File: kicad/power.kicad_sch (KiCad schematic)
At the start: 49 parts, among them J4 TYPE-C-31-M-12, Q7 BC847BW,115, U10 MC34063AD, U11 MC34063AD, U12 XC6206P332MR-G, U13 TPS2116DRLR, U9 TPD4S012DRYR

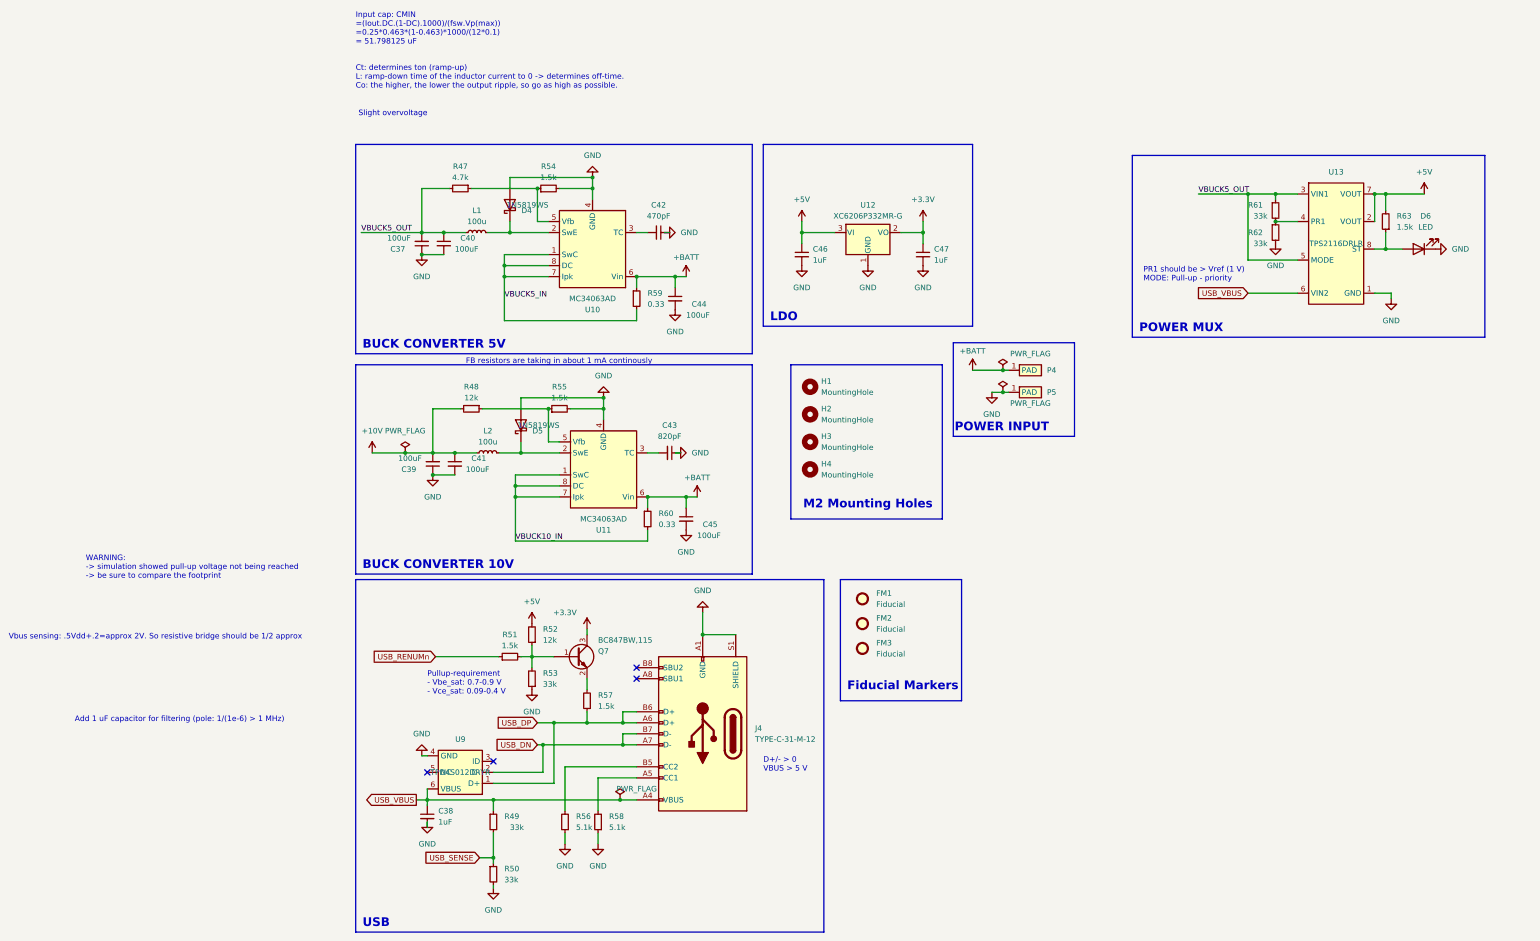
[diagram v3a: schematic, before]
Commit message: [kicad] Added different ESD protection device, silkscreen indication on the back, [review] Added pdf file and images of the front and back as well as 3d images
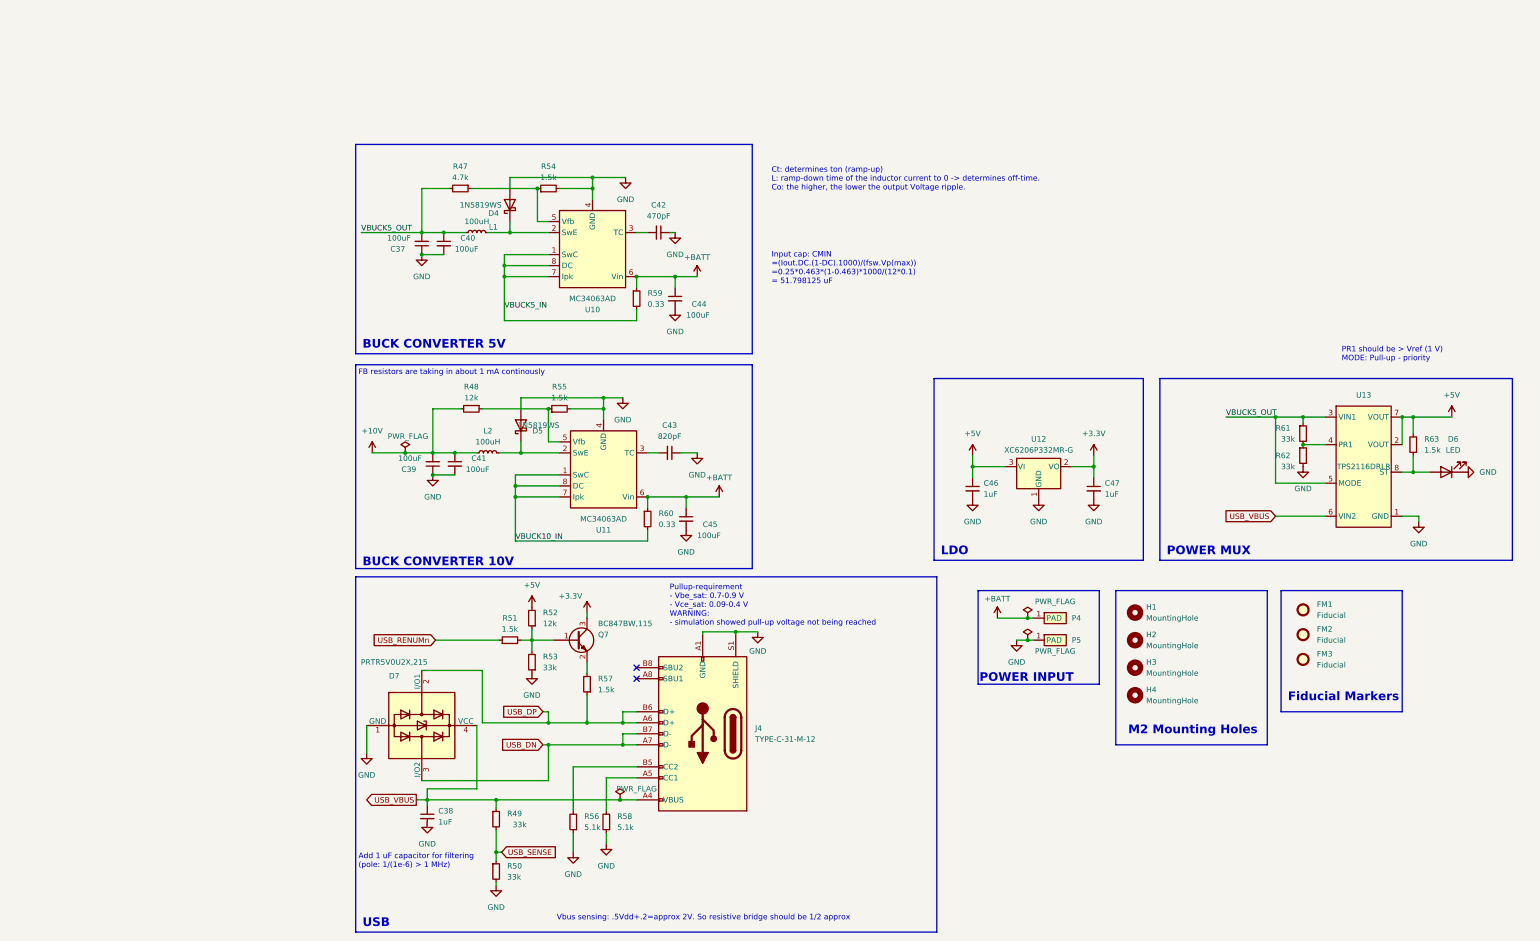
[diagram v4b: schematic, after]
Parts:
- removed U9: TPD4S012DRYR, bldc:TI_R-PUSON-N6, symbol bldc:TPD4S012DRYR
- added D7: PRTR5V0U2X,215, Package_TO_SOT_SMD:SOT-143, symbol Power_Protection:PRTR5V0U2X
- L1, L2: value 100u -> 100uH
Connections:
- net GND: now also D7.1 (GND)
- net USB_DN: now also D7.3 (I/O2)
- net USB_DP: now also D7.2 (I/O1)
- net USB_VBUS: now also D7.4 (VCC)
- no-connect marks 4 -> 2
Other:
- note added: "Ct: determines ton (ramp-up) L: ramp-down time of the inductor current to 0 -> determines off-time. Co: the higher, the lower the output Voltage ripple."
- note added: "Pullup-requirement - Vbe_sat: 0.7-0.9 V - Vce_sat: 0.09-0.4 V WARNING: - simulation showed pull-up voltage not being reached"
- note removed: "Ct: determines ton (ramp-up) L: ramp-down time of the inductor current to 0 -> determines off-time. Co: the higher, the lower the output ripple, so go as high as possible."
- note removed: "D+/- > 0 VBUS > 5 V"
- note removed: "Pullup-requirement - Vbe_sat: 0.7-0.9 V - Vce_sat: 0.09-0.4 V"
- note removed: "Slight overvoltage"
- note removed: "WARNING: -> simulation showed pull-up voltage not being reached -> be sure to compare the footprint"
- company: Igor Wolfs -> IW
- moved on the sheet: C46, C47, D6, FM1, FM2, FM3, H1, H2, H3, H4, P4, P5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

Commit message: [kicad] Added testpoints, added 1 amp fuses at 2 buck converters
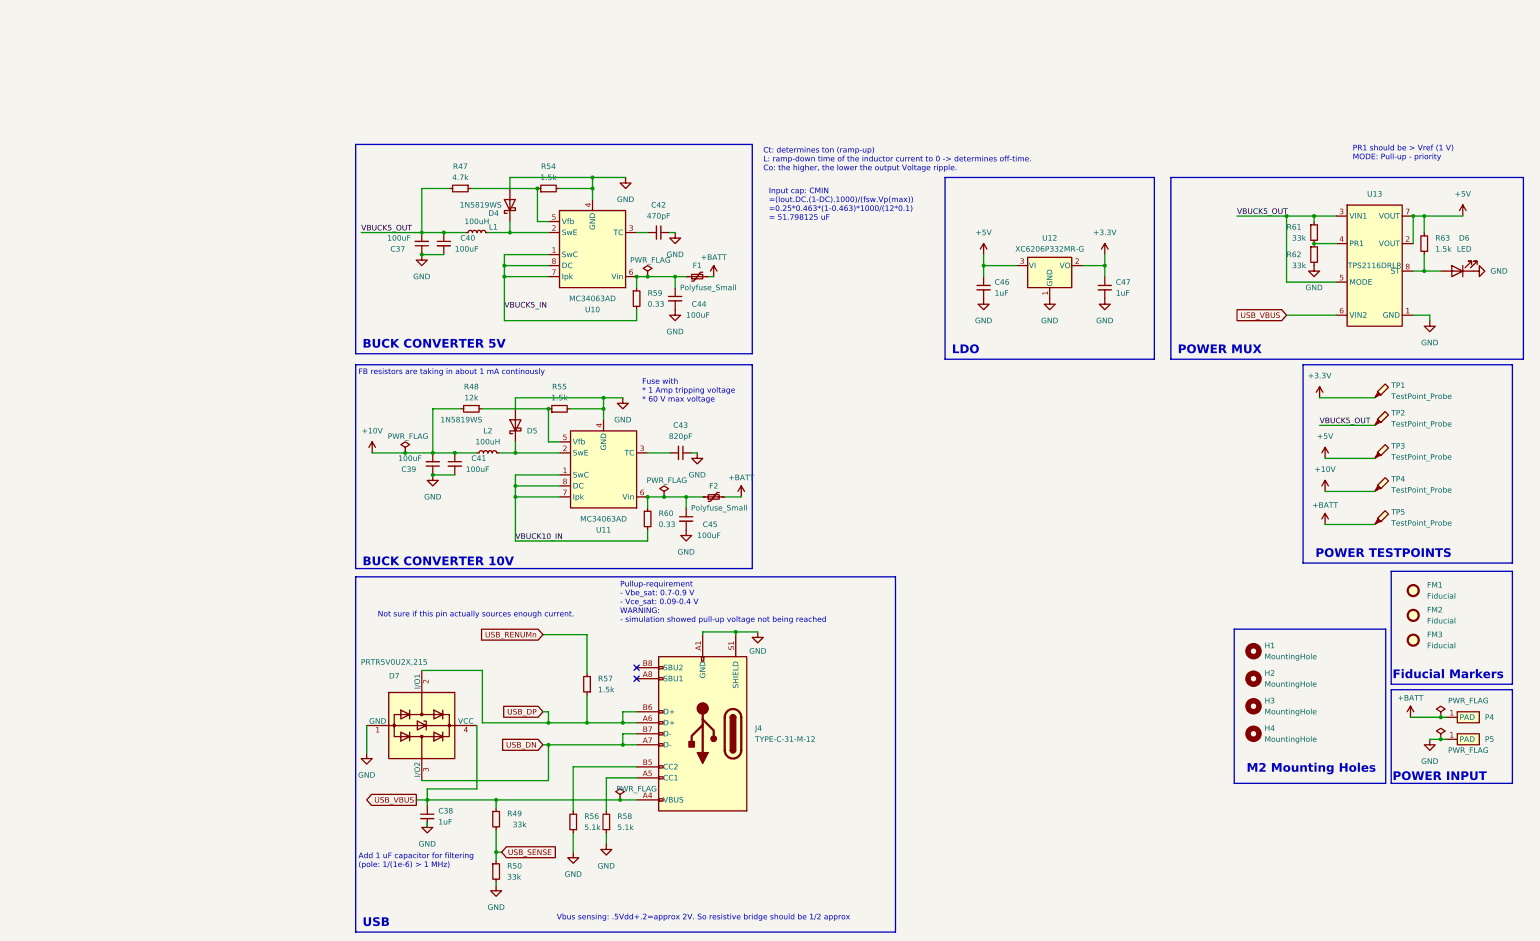
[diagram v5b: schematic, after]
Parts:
- removed Q7: BC847BW,115, Package_TO_SOT_SMD:SOT-323_SC-70, symbol Transistor_BJT:BC847
- removed R51: 1.5k, Resistor_SMD:R_0805_2012Metric, symbol Device:R_Small
- removed R52: 12k, Resistor_SMD:R_0603_1608Metric, symbol Device:R_Small
- removed R53: 33k, Resistor_SMD:R_0603_1608Metric, symbol Device:R_Small
- added F1, F2: Polyfuse_Small, Fuse:Fuse_1812_4532Metric, symbol Device:Polyfuse_Small
- added TP1, TP2, TP3, TP4, TP5: TestPoint_Probe, TestPoint:TestPoint_THTPad_D1.0mm_Drill0.5mm, symbol Connector:TestPoint_Probe
- C42, C43: footprint Capacitor_SMD:C_0805_2012Metric -> Capacitor_SMD:C_0805_2012Metric_Pad1.18x1.45mm_HandSolder
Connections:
- net +10V: now also TP4.1
- net +3.3V: now also TP1.1
- net +5V: now also TP3.1
- net +BATT: now also F1.2, F2.2, TP5.1; no longer C44.1, C45.1, R59.1, R60.1, U10.6 (Vin), U11.6 (Vin)
- net USB_RENUMn: now also R57.2
- net VBUCK5_OUT: now also TP2.1
- new net: C45.1, F2.1, R60.1, U11.6 (Vin)
- new net: C44.1, F1.1, R59.1, U10.6 (Vin)
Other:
- note added: "Fuse with * 1 Amp tripping voltage * 60 V max voltage"
- note added: "Not sure if this pin actually sources enough current."
- moved on the sheet: C43, C46, C47, D5, D6, FM1, FM2, FM3, H1, H2, H3, H4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

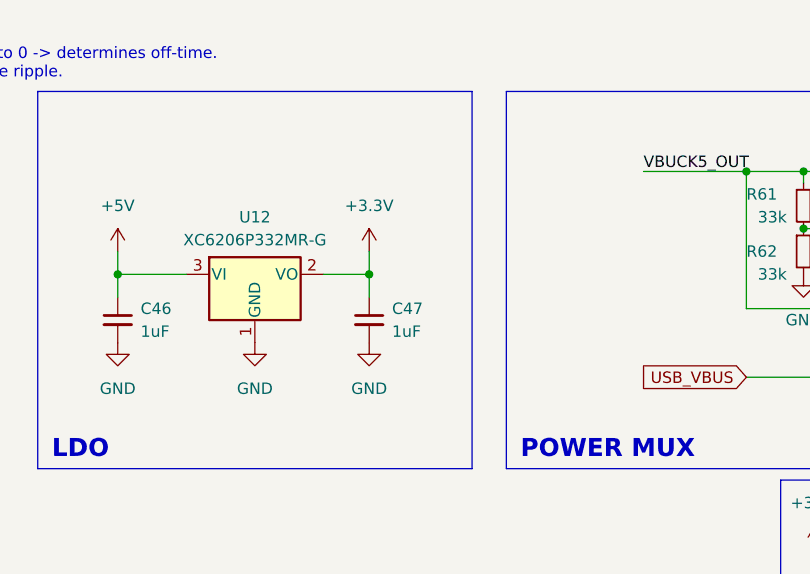
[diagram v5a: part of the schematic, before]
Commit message: [kicad] Added power and keepalive LED | TODO: Add extra mcu output
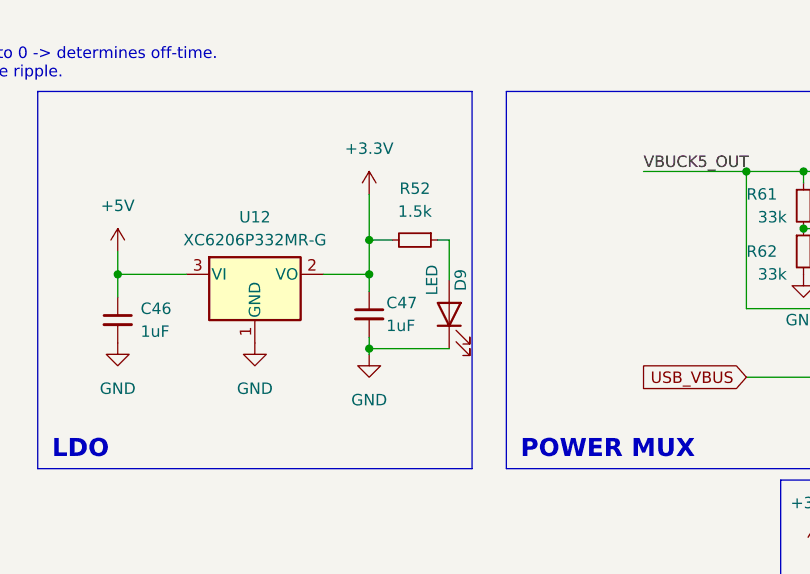
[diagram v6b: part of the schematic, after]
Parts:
- added D9: LED, LED_SMD:LED_0805_2012Metric, symbol Device:LED
- added R52: 1.5k, Resistor_SMD:R_0805_2012Metric, symbol Device:R_Small
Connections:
- net +3.3V: now also R52.2
- net GND: now also D9.1 (K)
- new net: D9.2 (A), R52.1
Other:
- moved on the sheet: C47
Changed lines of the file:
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@@
   (junction (at 50.8 34.29) (diameter 0) (color 0 0 0 0)
   )
+  (junction (at 187.96 38.1) (diameter 0) (color 0 0 0 0)
+  )
   (junction (at 52.07 85.09) (diameter 0) (color 0 0 0 0)
   )
@@
   )
   (junction (at 33.02 85.09) (diameter 0) (color 0 0 0 0)
+  )
+  (junction (at 187.96 50.165) (diameter 0) (color 0 0 0 0)
   )
   (junction (at 91.44 95.25) (diameter 0) (color 0 0 0 0)
@@
     (stroke (width 0) (type default))
   )
+  (wire (pts (xy 187.96 50.8) (xy 187.96 50.165))
+    (stroke (width 0) (type default))
+  )
   (wire (pts (xy 77.47 21.59) (xy 69.85 21.59))
     (stroke (width 0) (type default))
@@
     (stroke (width 0) (type default))
   )
+  (wire (pts (xy 187.96 50.165) (xy 187.96 48.895))
+    (stroke (width 0) (type default))
+  )
   (wire (pts (xy 52.07 105.41) (xy 52.07 95.25))
     (stroke (width 0) (type default))
@@
     (stroke (width 0) (type default))
   )
+  (wire (pts (xy 195.58 38.1) (xy 196.85 38.1))
+    (stroke (width 0) (type default))
+  )
   (wire (pts (xy 266.7 151.13) (xy 265.43 151.13))
     (stroke (width 0) (type default))
@@
     (stroke (width 0) (type default))
   )
+  (wire (pts (xy 187.96 38.1) (xy 187.96 41.91))
+    (stroke (width 0) (type default))
+  )
   (wire (pts (xy 33.02 85.09) (xy 38.1 85.09))
     (stroke (width 0) (type default))
@@
     (stroke (width 0) (type default))
   )
+  (wire (pts (xy 187.96 50.165) (xy 196.85 50.165))
+    (stroke (width 0) (type default))
+  )
   (wire (pts (xy 52.07 105.41) (xy 82.55 105.41))
     (stroke (width 0) (type default))
@@
     (stroke (width 0) (type default))
   )
-  (wire (pts (xy 187.96 41.91) (xy 187.96 44.45))
+  (wire (pts (xy 187.96 41.91) (xy 187.96 43.815))
     (stroke (width 0) (type default))
   )
@@
     (stroke (width 0) (type default))
   )
+  (wire (pts (xy 196.85 38.1) (xy 196.85 42.545))
+    (stroke (width 0) (type default))
+  )
   (wire (pts (xy 82.55 102.87) (xy 82.55 105.41))
     (stroke (width 0) (type default))
@@
     (stroke (width 0) (type default))
   )
-  (wire (pts (xy 187.96 39.37) (xy 187.96 41.91))
+  (wire (pts (xy 187.96 33.02) (xy 187.96 38.1))
+    (stroke (width 0) (type default))
+  )
+  (wire (pts (xy 187.96 38.1) (xy 190.5 38.1))
     (stroke (width 0) (type default))
   )
@@
     )
   )
-  (symbol (lib_id "Device:C_Small") (at 187.96 46.99 0) (unit 1)
-    (in_bom yes) (on_board yes) (dnp no) (fields_autoplaced)
-    (property "Reference" "C47" (at 190.5 45.7263 0)
-      (effects (font (size 1.27 1.27)) (justify left))
-    )
-    (property "Value" "1uF" (at 190.5 48.2663 0)
-      (effects (font (size 1.27 1.27)) (justify left))
-    )
-    (property "Footprint" "Capacitor_SMD:C_1206_3216Metric" (at 187.96 46.99 0)
-      (effects (font (size 1.27 1.27)) hide)
-    )
-    (property "Datasheet" "https://wmsc.lcsc.com/wmsc/upload/file/pdf/v2/lcsc/2304140030_Samsung-Electro-Mechanics-CL31B105KBHNNNE_C1848.pdf" (at 187.96 46.99 0)
-      (effects (font (size 1.27 1.27)) hide)
-    )
-    (property "jlcpcb" "C1848" (at 187.96 46.99 0)
-      (effects (font (size 1.27 1.27)) hide)
-    )
-    (property "MFR.Part" "CL31B105KBHNNNE" (at 187.96 46.99 0)
+  (symbol (lib_id "Device:C_Small") (at 187.96 46.355 0) (unit 1)
+    (in_bom yes) (on_board yes) (dnp no)
+    (property "Reference" "C47" (at 189.865 45.085 0)
+      (effects (font (size 1.27 1.27)) (justify left))
+    )
+    (property "Value" "1uF" (at 189.865 47.625 0)
+      (effects (font (size 1.27 1.27)) (justify left))
+    )
+    (property "Footprint" "Capacitor_SMD:C_1206_3216Metric" (at 187.96 46.355 0)
+      (effects (font (size 1.27 1.27)) hide)
+    )
+    (property "Datasheet" "https://wmsc.lcsc.com/wmsc/upload/file/pdf/v2/lcsc/2304140030_Samsung-Electro-Mechanics-CL31B105KBHNNNE_C1848.pdf" (at 187.96 46.355 0)
+      (effects (font (size 1.27 1.27)) hide)
+    )
+    (property "jlcpcb" "C1848" (at 187.96 46.355 0)
+      (effects (font (size 1.27 1.27)) hide)
+    )
+    (property "MFR.Part" "CL31B105KBHNNNE" (at 187.96 46.355 0)
       (effects (font (size 1.27 1.27)) hide)
     )
@@
         (path "/91e2f46a-700b-4d7a-a06a-22469f63223f/53dc30ee-9af6-4771-8676-c78726df5d90"
           (reference "L2") (unit 1)
+        )
+      )
+    )
+  )
+  (symbol (lib_id "Device:LED") (at 196.85 46.355 90) (unit 1)
+    (in_bom yes) (on_board yes) (dnp no)
+    (property "Reference" "D9" (at 198.12 42.545 0)
+      (effects (font (size 1.27 1.27)))
+    )
+    (property "Value" "LED" (at 194.945 42.545 0)
+      (effects (font (size 1.27 1.27)))
+    )
+    (property "Footprint" "LED_SMD:LED_0805_2012Metric" (at 196.85 46.355 0)
+      (effects (font (size 1.27 1.27)) hide)
+    )
+    (property "Datasheet" "https://wmsc.lcsc.com/wmsc/upload/file/pdf/v2/lcsc/2106081832_baizou-BZ-C0805-Y2-E1_C2833070.pdf" (at 196.85 46.355 0)
+      (effects (font (size 1.27 1.27)) hide)
+    )
+    (property "jlcpcb" "C2833070" (at 196.85 46.355 0)
+      (effects (font (size 1.27 1.27)) hide)
+    )
+    (property "MFR.Part" "BZ-C0805-Y2-E1" (at 196.85 46.355 0)
+      (effects (font (size 1.27 1.27)) hide)
+    )
+    (pin "1")
+    (pin "2")
+    (instances
+      (project "bldc_project"
+        (path "/91e2f46a-700b-4d7a-a06a-22469f63223f/53dc30ee-9af6-4771-8676-c78726df5d90"
+          (reference "D9") (unit 1)
         )
       )
@@
     )
   )
+  (symbol (lib_id "Device:R_Small") (at 193.04 38.1 270) (unit 1)
+    (in_bom yes) (on_board yes) (dnp no) (fields_autoplaced)
+    (property "Reference" "R52" (at 193.04 32.385 90)
+      (effects (font (size 1.27 1.27)))
+    )
+    (property "Value" "1.5k" (at 193.04 34.925 90)
+      (effects (font (size 1.27 1.27)))
+    )
+    (property "Footprint" "Resistor_SMD:R_0805_2012Metric" (at 193.04 38.1 0)
+      (effects (font (size 1.27 1.27)) hide)
+    )
+    (property "Datasheet" "https://wmsc.lcsc.com/wmsc/upload/file/pdf/v2/lcsc/2206010216_UNI-ROYAL-Uniroyal-Elec-0805W8F1501T5E_C4310.pdf" (at 193.04 38.1 0)
+      (effects (font (size 1.27 1.27)) hide)
+    )
+    (property "jlcpcb" "C4310" (at 193.04 38.1 0)
+      (effects (font (size 1.27 1.27)) hide)
+    )
+    (property "MFR.Part" "0805W8F1501T5E" (at 193.04 38.1 0)
+      (effects (font (size 1.27 1.27)) hide)
+    )
+    (pin "2")
+    (pin "1")
+    (instances
+      (project "bldc_project"
+        (path "/91e2f46a-700b-4d7a-a06a-22469f63223f/53dc30ee-9af6-4771-8676-c78726df5d90"
+          (reference "R52") (unit 1)
+        )
+      )
+    )
+  )
   (symbol (lib_id "power:GND") (at 107.95 126.365 0) (unit 1)
     (in_bom yes) (on_board yes) (dnp no) (fields_autoplaced)
@@
     )
   )
-  (symbol (lib_id "power:+3.3V") (at 187.96 39.37 0) (unit 1)
-    (in_bom yes) (on_board yes) (dnp no) (fields_autoplaced)
-    (property "Reference" "#PWR082" (at 187.96 43.18 0)
-      (effects (font (size 1.27 1.27)) hide)
-    )
-    (property "Value" "+3.3V" (at 187.96 34.29 0)
-      (effects (font (size 1.27 1.27)))
-    )
-    (property "Footprint" "" (at 187.96 39.37 0)
-      (effects (font (size 1.27 1.27)) hide)
-    )
-    (property "Datasheet" "" (at 187.96 39.37 0)
+  (symbol (lib_id "power:+3.3V") (at 187.96 33.02 0) (unit 1)
+    (in_bom yes) (on_board yes) (dnp no) (fields_autoplaced)
+    (property "Reference" "#PWR082" (at 187.96 36.83 0)
+      (effects (font (size 1.27 1.27)) hide)
+    )
+    (property "Value" "+3.3V" (at 187.96 27.94 0)
+      (effects (font (size 1.27 1.27)))
+    )
+    (property "Footprint" "" (at 187.96 33.02 0)
+      (effects (font (size 1.27 1.27)) hide)
+    )
+    (property "Datasheet" "" (at 187.96 33.02 0)
       (effects (font (size 1.27 1.27)) hide)
     )
@@
     )
   )
-  (symbol (lib_id "power:GND") (at 187.96 49.53 0) (unit 1)
-    (in_bom yes) (on_board yes) (dnp no) (fields_autoplaced)
-    (property "Reference" "#PWR083" (at 187.96 55.88 0)
-      (effects (font (size 1.27 1.27)) hide)
-    )
-    (property "Value" "GND" (at 187.96 54.61 0)
-      (effects (font (size 1.27 1.27)))
-    )
-    (property "Footprint" "" (at 187.96 49.53 0)
-      (effects (font (size 1.27 1.27)) hide)
-    )
-    (property "Datasheet" "" (at 187.96 49.53 0)
-      (effects (font (size 1.27 1.27)) hide)
-    )
+  (symbol (lib_id "power:GND") (at 187.96 50.8 0) (unit 1)
+    (in_bom yes) (on_board yes) (dnp no) (fields_autoplaced)
+    (property "Reference" "#PWR083" (at 187.96 57.15 0)
+      (effects (font (size 1.27 1.27)) hide)
+    )
+    (property "Value" "GND" (at 187.96 55.88 0)
+      (effects (font (size 1.27 1.27)))
+    )
+    (property "Footprint" "" (at 187.96 50.8 0)
+      (effects (font (size 1.27 1.27)) hide)
+    )
+    (property "Datasheet" "" (at 187.96 50.8 0)
+      (effects (font (size 1.27 1.27)) hide)
+    )
